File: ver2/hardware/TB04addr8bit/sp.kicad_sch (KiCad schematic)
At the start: 7 parts, among them U16 74HC00, U39 74HC193, U40 74HC00, U41 74LS32, U42 74AHC04, U43 74LS08

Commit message: ver2: 回路図の要修正5件を修正しアノテーションを掛け直し
- 74HC193(旧U39/新U38)の~CO・~BOをVDD直結から開放に(出力短絡の回避)
- 電源未接続だった4IC(74HC00/74LS32/74AHC04/74LS08)にVCC/GNDを配線
  し、バイパスコンデンサ0.1u×4を追加
- ネット名 Decord を DCR に統一(デコーダ制御信号のラッチ不成立を解消)
- PC_LAOD の綴りを PC_LOAD に修正
- 書込デコーダ138の入力を OPR8-10 から sel_a0-2 へ付け替え
  (LD Ri,[Im8] が別レジスタに書く不具合の解消)
- ver1基板由来だった参照記号をアノテーション掛け直しで整理
  (部品216個・名前付きネット146本とも掛け直し前後で一致、ERCも同数)
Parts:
- added C53, C54, C55, C56: 0.1u, symbol Device:C
- renumbered C49 to C52, U42 to U2, U43 to U35, U40 to U36, U41 to U37, U39 to U38, U16 to U5
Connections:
- net GND: now also U2.7 (GND), U35.7 (GND), U36.7 (GND), U37.7 (GND), C53.1, C54.1, C55.1, C56.1
- net VDD: now also U2.14 (VCC), U35.14 (VCC), U36.14 (VCC), U37.14 (VCC), C53.2, C54.2, C55.2, C56.2; no longer U38.12 (~{CO}), U38.13 (~{BO})
- no-connect marks 1 -> 3
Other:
- moved on the sheet: U2B, U2C, U2D, U2E, U2F, U2G, U35E, U36A, U36E, U37C, U37D, U37E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

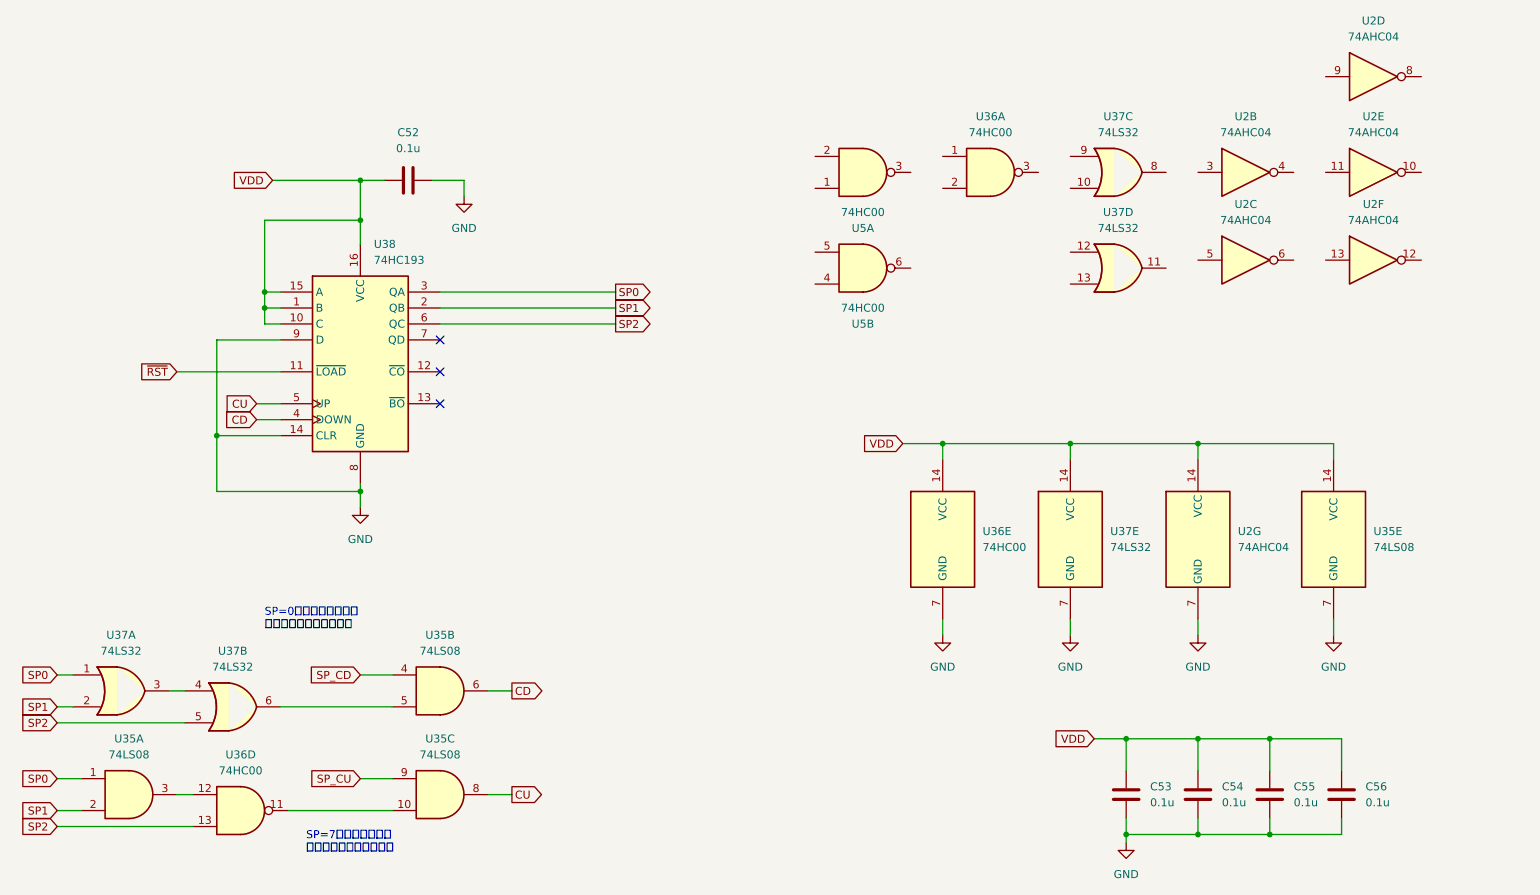
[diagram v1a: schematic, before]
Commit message: ver2: SPのCU/CDに相ゲートを追加、74HC00の電源ユニットを置き直し
- CU=NAND(DCR, SP_CU&!(SP==7)) / CD=NAND(EXE, SP_CD&(SP!=0)) とし、
  74HC193をアイドルHigh・相の終わりの立ち上がりで1回だけ数える形に変更
  (POP/RETはDCR末のpre-inc、PUSH/CALLはEXE末のpost-dec)
  従来のAND直結ではPUSHがpre-decになり、連続PUSH/POPで
  レベルが継続して2回目のカウントを取りこぼす問題があった
- 空いていた74HC00(U5)の2ゲートを使用。spシートのERCが6件減少
- 74HC00の電源ユニット(U5E)をver1由来の残骸ごと削除しsp側へ置き直し
  (ルートに (project "" reference "U16") が残り電源ユニット未配置扱いだった)
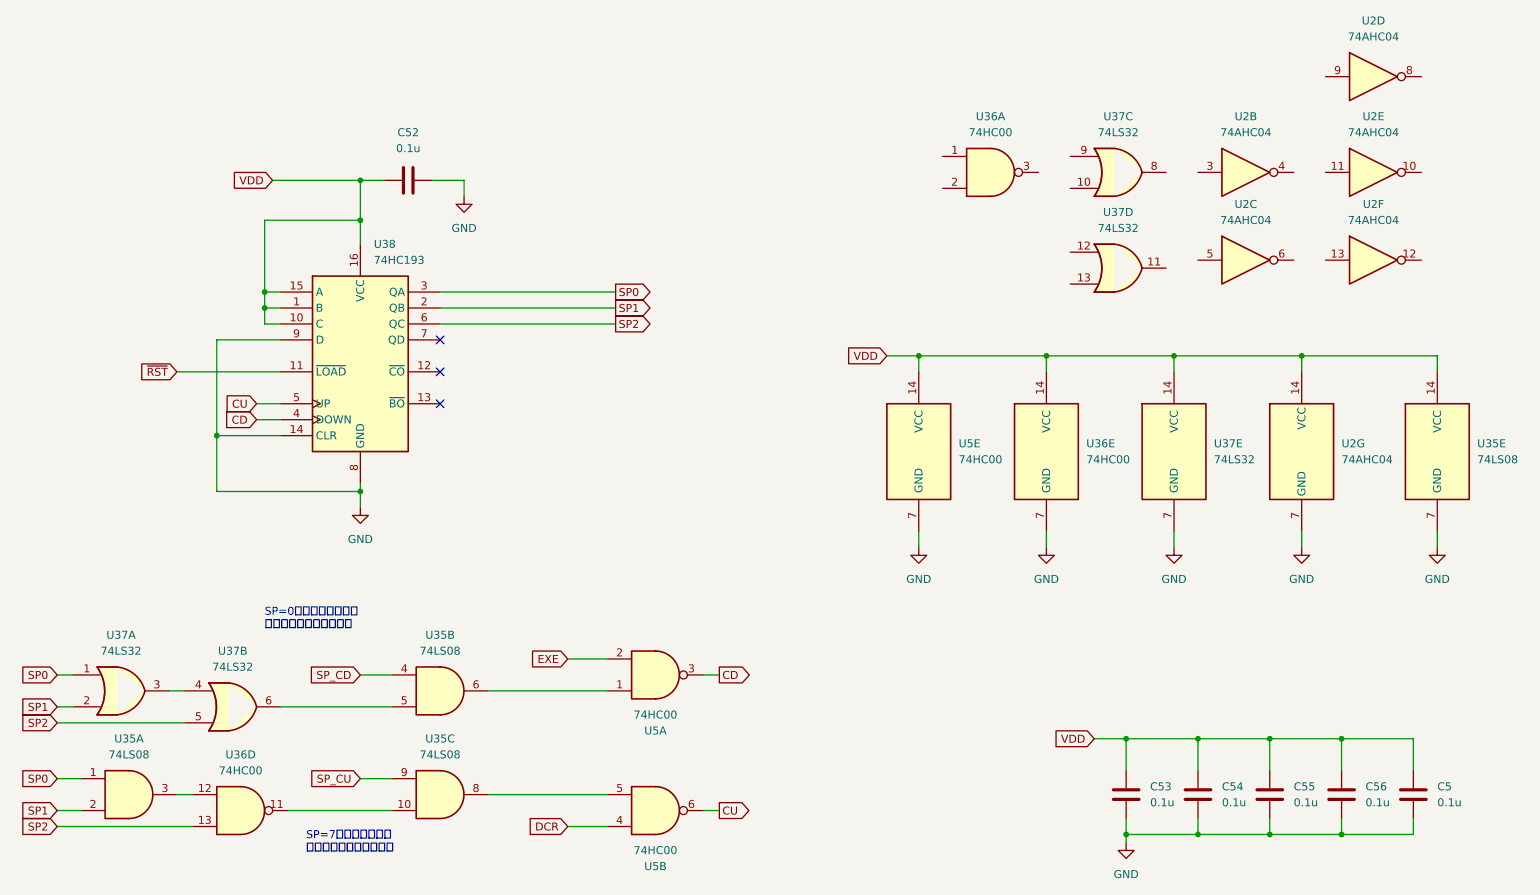
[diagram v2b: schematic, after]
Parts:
- added C5: 0.1u, Capacitor_THT:C_Disc_D4.3mm_W1.9mm_P5.00mm, symbol Device:C
- added unit 5 of U5
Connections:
- net CD: now also U5.3; no longer U35.6
- net CU: now also U5.6; no longer U35.8
- net GND: now also C5.2, U5.7 (GND)
- net VDD: now also C5.1, U5.14 (VCC)
- net DCR: now reaches U5.4
- net at U5.5: now also U35.8
- net at U5.1: now also U35.6
- net EXE: now reaches U5.2
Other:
- moved on the sheet: U2G, U35E, U36E, U37E, U5A, U5B

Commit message: ver2: addrMUXシートを新設、リセット起点をFCH1へ、mAddr専用レジスタを廃止
- addrMUX.kicad_sch を新設。74HC138(U41)で SEL_M からアドレス源の
  イネーブルをワンホット生成し、74HC244×5(U42-U46)を配置
  mAddr用(U43)の入力は byte2ラッチのOPR4-11から直取り
- mAddr専用レジスタ(IC11/IC12)を削除。byte2ラッチが mAddr を兼ねる
  これまで消費先ゼロだった OPR7/OPR11 の浮きも解消
- 74HC238の出力割付を1つ回してリセット起点を EXE から FCH1 へ
  (Y0=FCH1/Y1=FCH2/Y2=DCR/Y3=EXE、相順は不変)
- PCの161はCEPを共通イネーブルに揃え、桁上げをTC->CETで接続

未了: 命令ラッチの取り込みエッジを1相ずらす変更(U20 Cp=FCH2 /
U26 Cp=DCR)。EXE中はアドレスバスがmAddrのため、現状のままでは
EXE->FCH1の境目でROMのアクセスが間に合わない
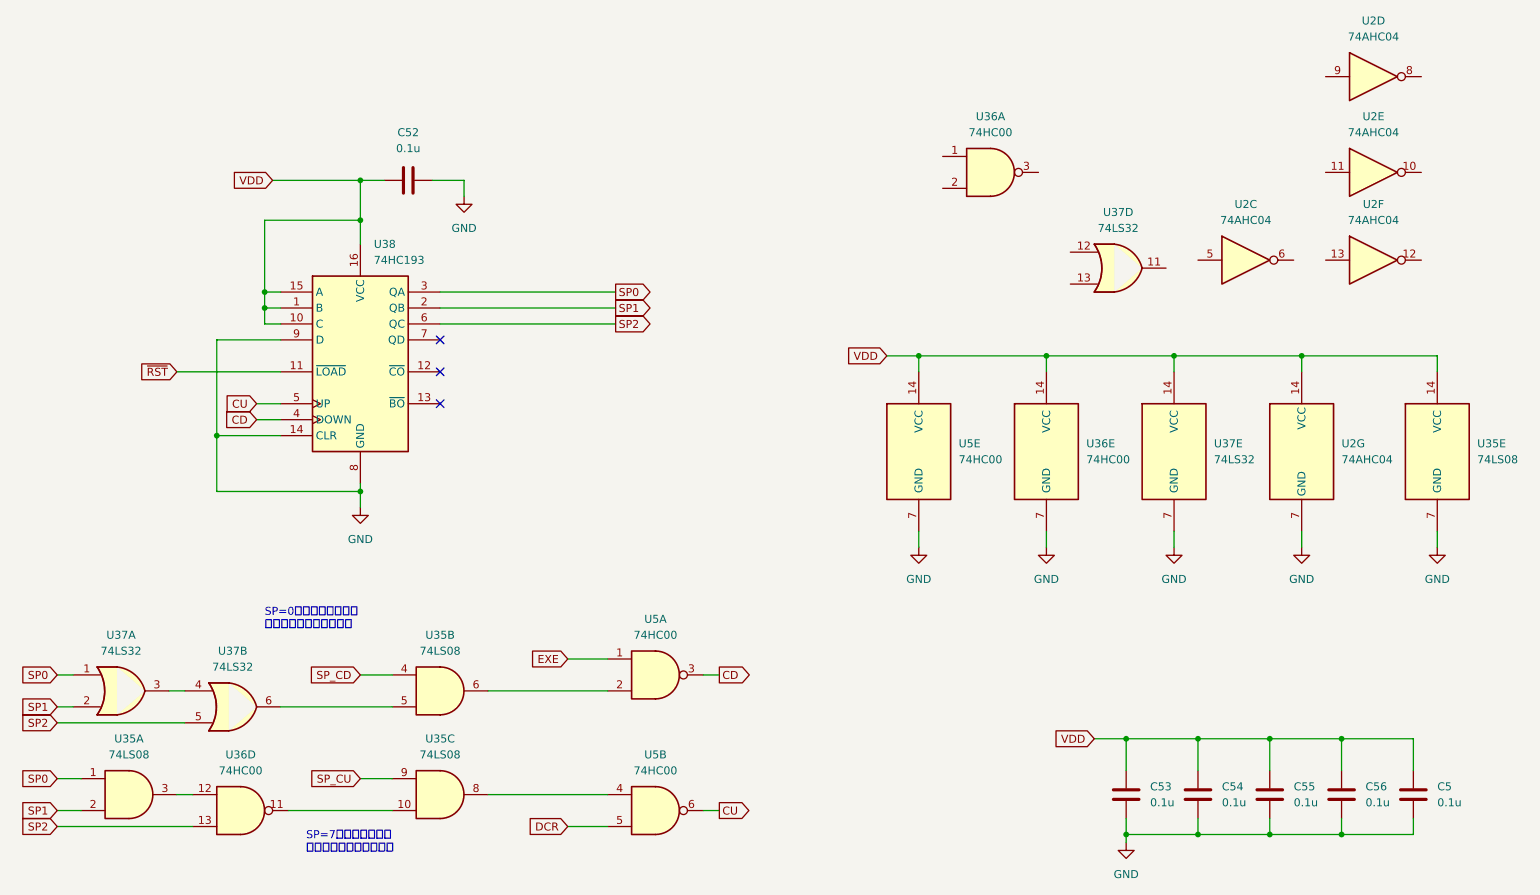
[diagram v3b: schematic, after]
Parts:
- removed unit 2 of U2
- removed unit 3 of U37
- U5: footprint Package_DIP:DIP-14_W7.62mm_Socket -> (none)
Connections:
- net DCR: now also U5.5; no longer U5.4
- net EXE: now also U5.1; no longer U5.2
- net at U35.8: now also U5.4; no longer U5.5
- net at U35.6: now also U5.2; no longer U5.1
